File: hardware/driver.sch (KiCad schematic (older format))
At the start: 11 parts, among them U1 74AC244, U2 74AC244, U3 74AC244, U4 ULN2803A

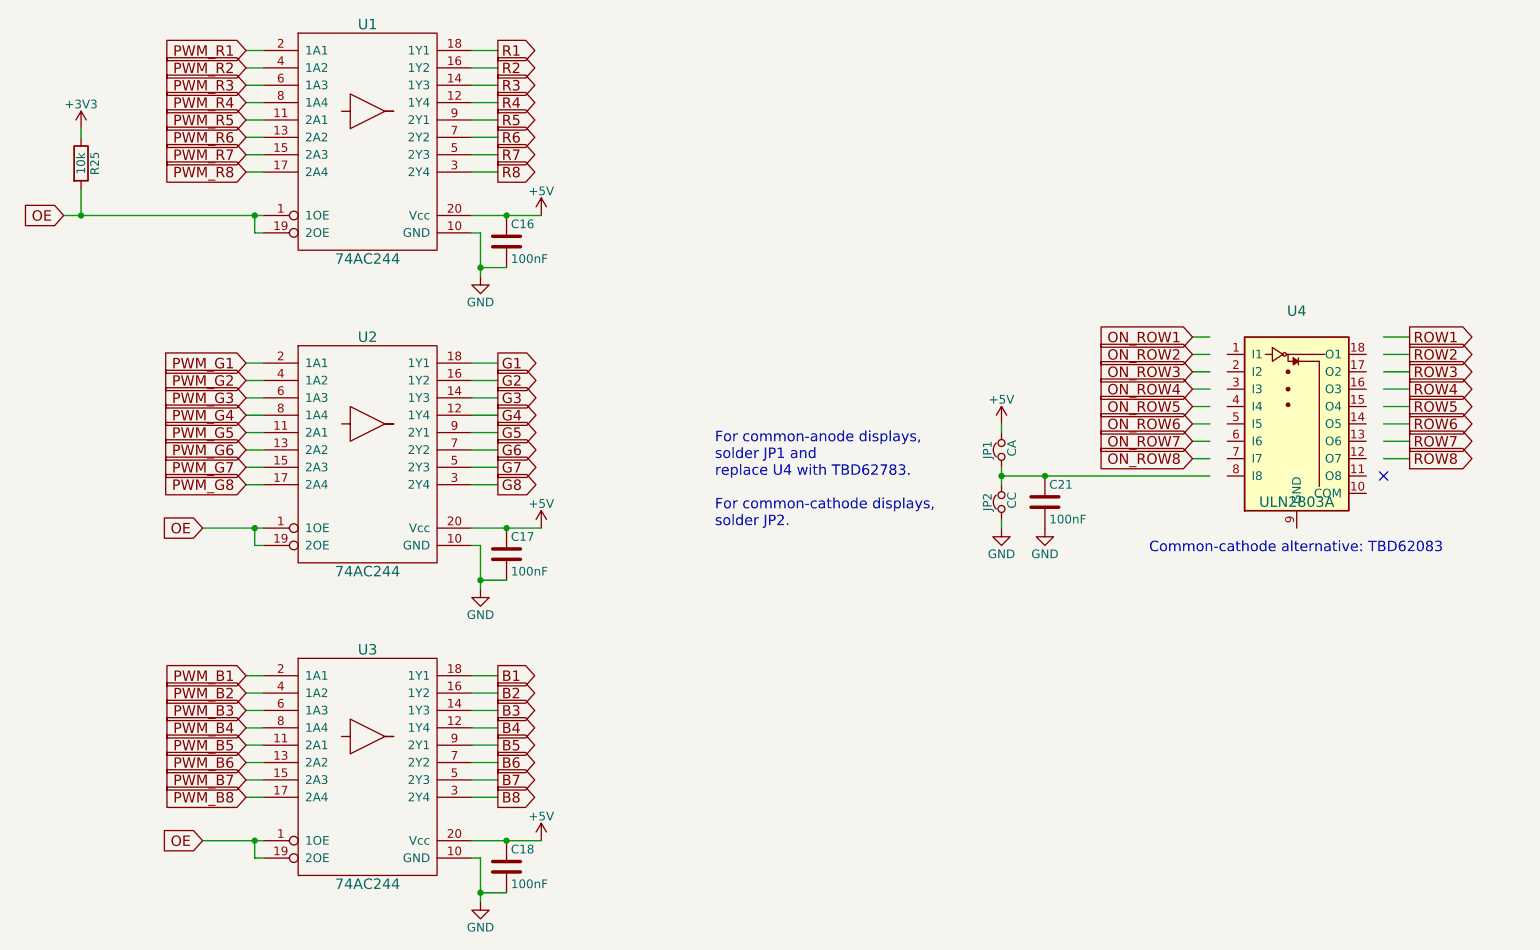
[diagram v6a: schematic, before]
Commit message: Update component versions (ULN2308A and USB_B)
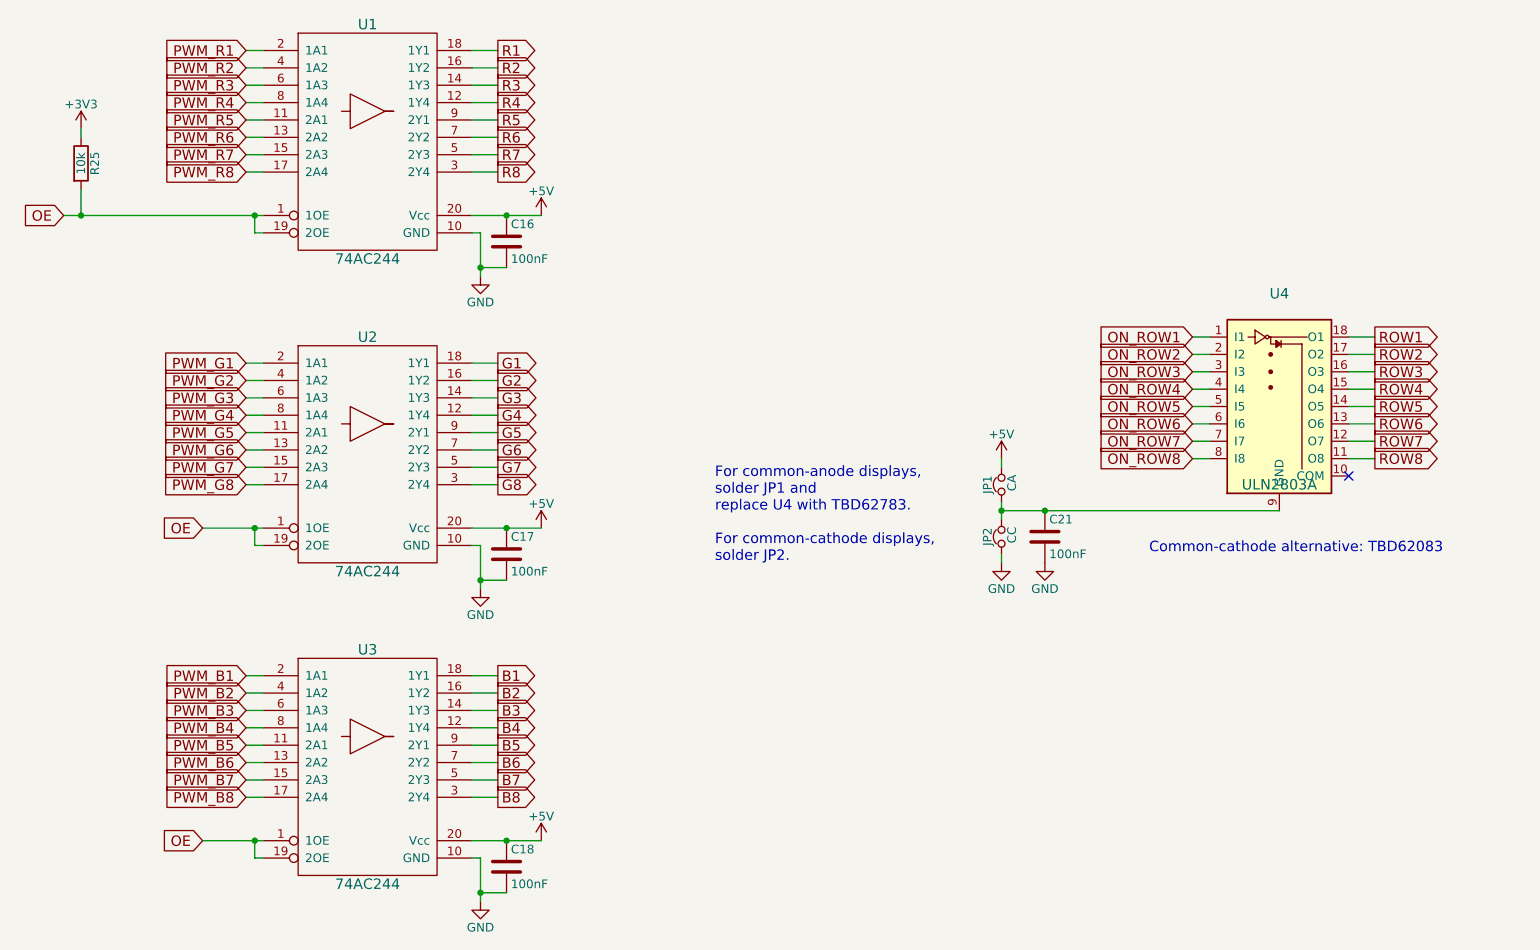
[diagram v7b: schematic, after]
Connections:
- wire segments 92 -> 104
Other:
- moved on the sheet: C21, JP1, JP2, U4
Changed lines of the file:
@@
 L ULN2803A U4
 U 1 1 580EA0CD
-P 8150 3700
-F 0 "U4" H 8150 4250 60  0000 C CNN
-F 1 "ULN2803A" H 8150 3150 60  0000 C CNN
-F 2 "Housings_SOIC:SOIC-18W_7.5x11.6mm_Pitch1.27mm" H 8150 4300 60  0001 C CNN
-F 3 "" H 8150 4300 60  0001 C CNN
-	1    8150 3700
-	1    0    0    -1
-$EndComp
-Text GLabel 8800 3300 2    60   Output ~ 0
+P 8050 3600
+AR Path="/580EA0CD" Ref="U4"  Part="1"
+AR Path="/580E2BF0/580EA0CD" Ref="U4"  Part="1"
+F 0 "U4" H 8050 4150 60  0000 C CNN
+F 1 "ULN2803A" H 8050 3050 60  0000 C CNN
+F 2 "Housings_SOIC:SOIC-18W_7.5x11.6mm_Pitch1.27mm" H 8050 4200 60  0001 C CNN
+F 3 "" H 8050 4200 60  0001 C CNN
+	1    8050 3600
+	1    0    0    -1
+$EndComp
+Text GLabel 8600 3300 2    60   Output ~ 0
 ROW1
-Text GLabel 8800 3400 2    60   Output ~ 0
+Text GLabel 8600 3400 2    60   Output ~ 0
 ROW2
-Text GLabel 8800 3500 2    60   Output ~ 0
+Text GLabel 8600 3500 2    60   Output ~ 0
 ROW3
-Text GLabel 8800 3600 2    60   Output ~ 0
+Text GLabel 8600 3600 2    60   Output ~ 0
 ROW4
-Text GLabel 8800 3700 2    60   Output ~ 0
+Text GLabel 8600 3700 2    60   Output ~ 0
 ROW5
-Text GLabel 8800 3800 2    60   Output ~ 0
+Text GLabel 8600 3800 2    60   Output ~ 0
 ROW6
-Text GLabel 8800 3900 2    60   Output ~ 0
+Text GLabel 8600 3900 2    60   Output ~ 0
 ROW7
-Text GLabel 8800 4000 2    60   Output ~ 0
+Text GLabel 8600 4000 2    60   Output ~ 0
 ROW8
-NoConn ~ 8650 4100
+NoConn ~ 8450 4100
 $Comp
 L GND #PWR04
 U 1 1 580EA8A7
-P 6450 4400
-F 0 "#PWR04" H 6450 4150 50  0001 C CNN
-F 1 "GND" H 6450 4250 50  0000 C CNN
-F 2 "" H 6450 4400 50  0000 C CNN
-F 3 "" H 6450 4400 50  0000 C CNN
-	1    6450 4400
+P 6450 4600
+F 0 "#PWR04" H 6450 4350 50  0001 C CNN
+F 1 "GND" H 6450 4450 50  0000 C CNN
+F 2 "" H 6450 4600 50  0000 C CNN
+F 3 "" H 6450 4600 50  0000 C CNN
+	1    6450 4600
 	1    0    0    -1
 $EndComp
@@
 L +5V #PWR09
 U 1 1 5874F556
-P 6450 3800
-F 0 "#PWR09" H 6450 3650 50  0001 C CNN
-F 1 "+5V" H 6450 3940 50  0000 C CNN
-F 2 "" H 6450 3800 50  0000 C CNN
-F 3 "" H 6450 3800 50  0000 C CNN
-	1    6450 3800
-	1    0    0    -1
-$EndComp
-Text Notes 4800 4400 0    60   ~ 0
+P 6450 4000
+F 0 "#PWR09" H 6450 3850 50  0001 C CNN
+F 1 "+5V" H 6450 4140 50  0000 C CNN
+F 2 "" H 6450 4000 50  0000 C CNN
+F 3 "" H 6450 4000 50  0000 C CNN
+	1    6450 4000
+	1    0    0    -1
+$EndComp
+Text Notes 4800 4600 0    60   ~ 0
 For common-anode displays,\nsolder JP1 and\nreplace U4 with TBD62783.\n\nFor common-cathode displays,\nsolder JP2.
 $Comp
@@
 L C C21
 U 1 1 58783112
-P 6700 4250
-F 0 "C21" H 6725 4350 50  0000 L CNN
-F 1 "100nF" H 6725 4150 50  0000 L CNN
-F 2 "rgb-matrix:C_0805" H 6738 4100 50  0001 C CNN
-F 3 "" H 6700 4250 50  0000 C CNN
-	1    6700 4250
+P 6700 4450
+F 0 "C21" H 6725 4550 50  0000 L CNN
+F 1 "100nF" H 6725 4350 50  0000 L CNN
+F 2 "rgb-matrix:C_0805" H 6738 4300 50  0001 C CNN
+F 3 "" H 6700 4450 50  0000 C CNN
+	1    6700 4450
 	1    0    0    -1
 $EndComp
@@
 L GND #PWR010
 U 1 1 587832B7
-P 6700 4400
-F 0 "#PWR010" H 6700 4150 50  0001 C CNN
-F 1 "GND" H 6700 4250 50  0000 C CNN
-F 2 "" H 6700 4400 50  0000 C CNN
-F 3 "" H 6700 4400 50  0000 C CNN
-	1    6700 4400
+P 6700 4600
+F 0 "#PWR010" H 6700 4350 50  0001 C CNN
+F 1 "GND" H 6700 4450 50  0000 C CNN
+F 2 "" H 6700 4600 50  0000 C CNN
+F 3 "" H 6700 4600 50  0000 C CNN
+	1    6700 4600
 	1    0    0    -1
 $EndComp
@@
 	3400 2700 3450 2700
 Wire Wire Line
-	3450 2700 3450 2950
+	3450 2700 3450 2900
+Wire Wire Line
+	3450 2900 3450 2950
 Wire Wire Line
 	3550 2350 3400 2350
@@
 	2100 2350 2200 2350
 Wire Wire Line
-	3400 4400 3800 4400
+	3400 4400 3600 4400
+Wire Wire Line
+	3600 4400 3800 4400
 Wire Wire Line
 	3400 4500 3450 4500
 Wire Wire Line
-	3450 4500 3450 4750
-Wire Wire Line
-	1850 4400 2200 4400
+	3450 4500 3450 4700
+Wire Wire Line
+	3450 4700 3450 4750
+Wire Wire Line
+	1850 4400 2150 4400
+Wire Wire Line
+	2150 4400 2200 4400
 Wire Wire Line
 	2200 4500 2150 4500
@@
 	2100 4150 2200 4150
 Wire Wire Line
-	3400 6200 3800 6200
+	3400 6200 3600 6200
+Wire Wire Line
+	3600 6200 3800 6200
 Wire Wire Line
 	3400 6300 3450 6300
 Wire Wire Line
-	3450 6300 3450 6550
-Wire Wire Line
-	1850 6200 2200 6200
+	3450 6300 3450 6500
+Wire Wire Line
+	3450 6500 3450 6550
+Wire Wire Line
+	1850 6200 2150 6200
+Wire Wire Line
+	2150 6200 2200 6200
 Wire Wire Line
 	2200 6300 2150 6300
@@
 	2100 5950 2200 5950
 Wire Wire Line
-	8800 4000 8650 4000
-Wire Wire Line
-	8800 3300 8650 3300
-Wire Wire Line
-	8800 3400 8650 3400
-Wire Wire Line
-	8800 3500 8650 3500
-Wire Wire Line
-	8800 3600 8650 3600
-Wire Wire Line
-	8800 3700 8650 3700
-Wire Wire Line
-	8800 3800 8650 3800
-Wire Wire Line
-	8800 3900 8650 3900
+	8600 4000 8450 4000
+Wire Wire Line
+	8600 3300 8450 3300
+Wire Wire Line
+	8600 3400 8450 3400
+Wire Wire Line
+	8600 3500 8450 3500
+Wire Wire Line
+	8600 3600 8450 3600
+Wire Wire Line
+	8600 3700 8450 3700
+Wire Wire Line
+	8600 3800 8450 3800
+Wire Wire Line
+	8600 3900 8450 3900
 Wire Wire Line
 	7550 3300 7650 3300
@@
 Connection ~ 2150 6200
 Wire Wire Line
-	1050 2600 2200 2600
+	1050 2600 1150 2600
+Wire Wire Line
+	1150 2600 2150 2600
+Wire Wire Line
+	2150 2600 2200 2600
 Connection ~ 2150 2600
 Wire Wire Line
@@
 Connection ~ 1150 2600
 Wire Wire Line
-	3400 2600 3800 2600
+	3400 2600 3600 2600
+Wire Wire Line
+	3600 2600 3800 2600
 Wire Wire Line
 	3600 4700 3450 4700
@@
 Connection ~ 3450 6500
 Wire Wire Line
-	6450 4350 6450 4400
-Wire Wire Line
-	6450 3800 6450 3850
-Wire Wire Line
-	6700 4100 6700 4100
-Connection ~ 6700 4100
-Connection ~ 6450 4100
-Wire Wire Line
-	6450 4050 6450 4150
-Wire Wire Line
-	6450 4100 7650 4100
+	6450 4550 6450 4600
+Wire Wire Line
+	6450 4000 6450 4050
+Wire Wire Line
+	6700 4300 6700 4300
+Connection ~ 6700 4300
+Connection ~ 6450 4300
+Wire Wire Line
+	6450 4250 6450 4300
+Wire Wire Line
+	6450 4300 6450 4350
+Wire Wire Line
+	6450 4300 6700 4300
+Wire Wire Line
+	6700 4300 8050 4300
 $Comp
 L Jumper_NC_Small JP1
 U 1 1 58750A6A
-P 6450 3950
-F 0 "JP1" H 6450 4030 50  0000 C CNN
-F 1 "CA" H 6460 3890 50  0000 C CNN
-F 2 "rgb-matrix:SMD-solder-bridge-1mm" H 6450 3950 50  0001 C CNN
-F 3 "" H 6450 3950 50  0000 C CNN
-	1    6450 3950
+P 6450 4150
+F 0 "JP1" H 6450 4230 50  0000 C CNN
+F 1 "CA" H 6460 4090 50  0000 C CNN
+F 2 "rgb-matrix:SMD-solder-bridge-1mm" H 6450 4150 50  0001 C CNN
+F 3 "" H 6450 4150 50  0000 C CNN
+	1    6450 4150
 	0    -1   -1   0
 $EndComp
@@
 L Jumper_NC_Small JP2
 U 1 1 5875096F
-P 6450 4250
-F 0 "JP2" H 6450 4330 50  0000 C CNN
-F 1 "CC" H 6460 4190 50  0000 C CNN
-F 2 "rgb-matrix:SMD-solder-bridge-1mm" H 6450 4250 50  0001 C CNN
-F 3 "" H 6450 4250 50  0000 C CNN
-	1    6450 4250
+P 6450 4450
+F 0 "JP2" H 6450 4530 50  0000 C CNN
+F 1 "CC" H 6460 4390 50  0000 C CNN
+F 2 "rgb-matrix:SMD-solder-bridge-1mm" H 6450 4450 50  0001 C CNN
+F 3 "" H 6450 4450 50  0000 C CNN
+	1    6450 4450
 	0    -1   -1   0
 $EndComp

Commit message: Update version to 1.1
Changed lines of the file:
@@
 Title "USB RGB Matrix"
 Date ""
-Rev "1.0"
+Rev "1.1"
 Comp ""
 Comment1 ""
@@
 	3400 2700 3450 2700
 Wire Wire Line
-	3450 2700 3450 2900
-Wire Wire Line
-	3450 2900 3450 2950
+	3450 2700 3450 2950
 Wire Wire Line
 	3550 2350 3400 2350
@@
 	2100 2350 2200 2350
 Wire Wire Line
-	3400 4400 3600 4400
-Wire Wire Line
-	3600 4400 3800 4400
+	3400 4400 3800 4400
 Wire Wire Line
 	3400 4500 3450 4500
 Wire Wire Line
-	3450 4500 3450 4700
-Wire Wire Line
-	3450 4700 3450 4750
-Wire Wire Line
-	1850 4400 2150 4400
-Wire Wire Line
-	2150 4400 2200 4400
+	3450 4500 3450 4750
+Wire Wire Line
+	1850 4400 2200 4400
 Wire Wire Line
 	2200 4500 2150 4500
@@
 	2100 4150 2200 4150
 Wire Wire Line
-	3400 6200 3600 6200
-Wire Wire Line
-	3600 6200 3800 6200
+	3400 6200 3800 6200
 Wire Wire Line
 	3400 6300 3450 6300
 Wire Wire Line
-	3450 6300 3450 6500
-Wire Wire Line
-	3450 6500 3450 6550
-Wire Wire Line
-	1850 6200 2150 6200
-Wire Wire Line
-	2150 6200 2200 6200
+	3450 6300 3450 6550
+Wire Wire Line
+	1850 6200 2200 6200
 Wire Wire Line
 	2200 6300 2150 6300
@@
 Connection ~ 2150 6200
 Wire Wire Line
-	1050 2600 1150 2600
-Wire Wire Line
-	1150 2600 2150 2600
-Wire Wire Line
-	2150 2600 2200 2600
+	1050 2600 2200 2600
 Connection ~ 2150 2600
 Wire Wire Line
@@
 Connection ~ 1150 2600
 Wire Wire Line
-	3400 2600 3600 2600
-Wire Wire Line
-	3600 2600 3800 2600
+	3400 2600 3800 2600
 Wire Wire Line
 	3600 4700 3450 4700
@@
 	6450 4000 6450 4050
 Wire Wire Line
-	6700 4300 6700 4300
+	6450 4300 8050 4300
 Connection ~ 6700 4300
 Connection ~ 6450 4300
 Wire Wire Line
-	6450 4250 6450 4300
-Wire Wire Line
-	6450 4300 6450 4350
-Wire Wire Line
-	6450 4300 6700 4300
-Wire Wire Line
-	6700 4300 8050 4300
+	6450 4250 6450 4350
 $Comp
 L Jumper_NC_Small JP1
